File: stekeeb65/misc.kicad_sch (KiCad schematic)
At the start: 16 parts, among them J0 Conn_02x03_Odd_Even, J1 TYPE-C-31-M12_13_EDITED, U0 WE-TVS-82400102

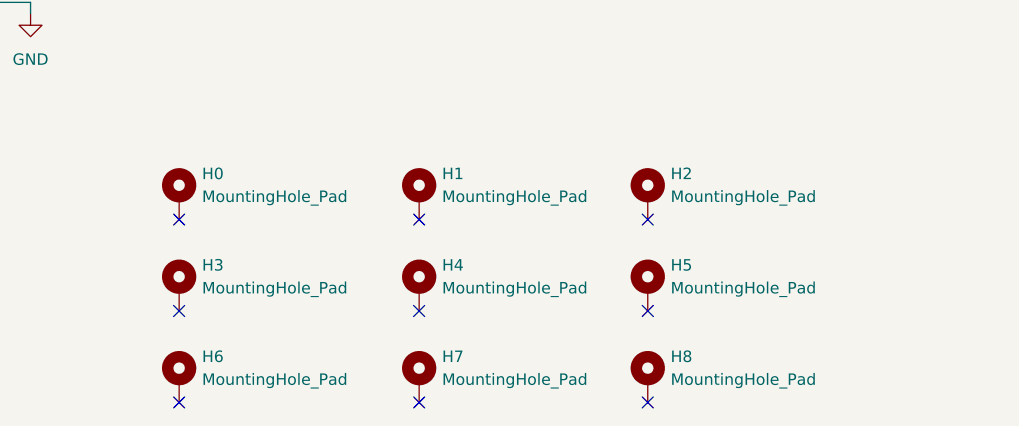
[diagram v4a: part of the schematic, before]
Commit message: Redoing keyboard layout. Adding flex cuts to PCB
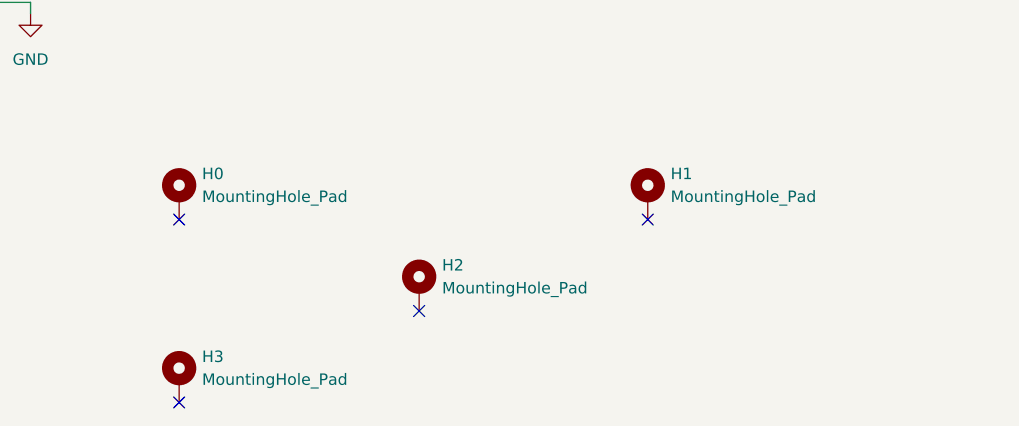
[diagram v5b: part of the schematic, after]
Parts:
- removed H1, H3, H5, H7, H8: MountingHole_Pad, MountingHole:MountingHole_2.2mm_M2_DIN965_Pad_TopOnly, symbol Mechanical:MountingHole_Pad
- F0: footprint Fuse:Fuse_0805_2012Metric_Pad1.15x1.40mm_HandSolder -> Fuse:Fuse_0603_1608Metric_Pad1.05x0.95mm_HandSolder
- H0: footprint MountingHole:MountingHole_2.2mm_M2_DIN965_Pad_TopOnly -> MountingHole:MountingHole_2.2mm_M2_DIN965_Pad_TopBottom
- H1: renamed from H2; footprint MountingHole:MountingHole_2.2mm_M2_DIN965_Pad_TopOnly -> MountingHole:MountingHole_2.2mm_M2_DIN965_Pad_TopBottom
- H2: renamed from H4; footprint MountingHole:MountingHole_2.2mm_M2_DIN965_Pad_TopOnly -> MountingHole:MountingHole_2.2mm_M2_DIN965_Pad_TopBottom
- H3: renamed from H6; footprint MountingHole:MountingHole_2.2mm_M2_DIN965_Pad_TopOnly -> MountingHole:MountingHole_2.2mm_M2_DIN965_Pad_TopBottom
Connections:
- no-connect marks 11 -> 6
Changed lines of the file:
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@@
   )
   (no_connect (at 91.44 135.89))
-  (no_connect (at 91.44 146.05))
-  (no_connect (at 116.84 135.89))
   (no_connect (at 116.84 125.73))
   (no_connect (at 64.77 125.73))
-  (no_connect (at 91.44 125.73))
   (no_connect (at 64.77 146.05))
-  (no_connect (at 116.84 146.05))
   (no_connect (at 54.61 92.71))
   (no_connect (at 54.61 90.17))
-  (no_connect (at 64.77 135.89))
   (wire (pts (xy 31.75 101.6) (xy 31.75 100.33))
     (stroke (width 0) (type default) (color 0 0 0 0))
@@
     (pin "1")
   )
-  (symbol (lib_id "Mechanical:MountingHole_Pad") (at 116.84 133.35 0) (unit 1)
-    (in_bom yes) (on_board yes) (fields_autoplaced)
-    (property "Reference" "H5" (id 0) (at 119.38 130.8099 0)
-      (effects (font (size 1.27 1.27)) (justify left))
-    )
-    (property "Value" "MountingHole_Pad" (id 1) (at 119.38 133.3499 0)
-      (effects (font (size 1.27 1.27)) (justify left))
-    )
-    (property "Footprint" "MountingHole:MountingHole_2.2mm_M2_DIN965_Pad_TopOnly" (id 2) (at 116.84 133.35 0)
-      (effects (font (size 1.27 1.27)) hide)
-    )
-    (property "Datasheet" "~" (id 3) (at 116.84 133.35 0)
-      (effects (font (size 1.27 1.27)) hide)
-    )
-    (pin "1")
-  )
   (symbol (lib_id "Mechanical:MountingHole_Pad") (at 64.77 123.19 0) (unit 1)
     (in_bom yes) (on_board yes) (fields_autoplaced)
@@
       (effects (font (size 1.27 1.27)) (justify left))
     )
-    (property "Footprint" "MountingHole:MountingHole_2.2mm_M2_DIN965_Pad_TopOnly" (id 2) (at 64.77 123.19 0)
+    (property "Footprint" "MountingHole:MountingHole_2.2mm_M2_DIN965_Pad_TopBottom" (id 2) (at 64.77 123.19 0)
       (effects (font (size 1.27 1.27)) hide)
     )
@@
     (pin "2")
   )
-  (symbol (lib_id "Mechanical:MountingHole_Pad") (at 91.44 123.19 0) (unit 1)
-    (in_bom yes) (on_board yes) (fields_autoplaced)
-    (property "Reference" "H1" (id 0) (at 93.98 120.6499 0)
-      (effects (font (size 1.27 1.27)) (justify left))
-    )
-    (property "Value" "MountingHole_Pad" (id 1) (at 93.98 123.1899 0)
-      (effects (font (size 1.27 1.27)) (justify left))
-    )
-    (property "Footprint" "MountingHole:MountingHole_2.2mm_M2_DIN965_Pad_TopOnly" (id 2) (at 91.44 123.19 0)
-      (effects (font (size 1.27 1.27)) hide)
-    )
-    (property "Datasheet" "~" (id 3) (at 91.44 123.19 0)
-      (effects (font (size 1.27 1.27)) hide)
-    )
-    (pin "1")
-  )
   (symbol (lib_id "power:+5V") (at 92.71 62.23 0) (unit 1)
     (in_bom yes) (on_board yes) (fields_autoplaced)
@@
   (symbol (lib_id "Mechanical:MountingHole_Pad") (at 91.44 133.35 0) (unit 1)
     (in_bom yes) (on_board yes) (fields_autoplaced)
-    (property "Reference" "H4" (id 0) (at 93.98 130.8099 0)
+    (property "Reference" "H2" (id 0) (at 93.98 130.8099 0)
       (effects (font (size 1.27 1.27)) (justify left))
     )
@@
       (effects (font (size 1.27 1.27)) (justify left))
     )
-    (property "Footprint" "MountingHole:MountingHole_2.2mm_M2_DIN965_Pad_TopOnly" (id 2) (at 91.44 133.35 0)
+    (property "Footprint" "MountingHole:MountingHole_2.2mm_M2_DIN965_Pad_TopBottom" (id 2) (at 91.44 133.35 0)
       (effects (font (size 1.27 1.27)) hide)
     )
@@
     (pin "1")
   )
-  (symbol (lib_id "Mechanical:MountingHole_Pad") (at 64.77 133.35 0) (unit 1)
-    (in_bom yes) (on_board yes) (fields_autoplaced)
-    (property "Reference" "H3" (id 0) (at 67.31 130.8099 0)
-      (effects (font (size 1.27 1.27)) (justify left))
-    )
-    (property "Value" "MountingHole_Pad" (id 1) (at 67.31 133.3499 0)
-      (effects (font (size 1.27 1.27)) (justify left))
-    )
-    (property "Footprint" "MountingHole:MountingHole_2.2mm_M2_DIN965_Pad_TopOnly" (id 2) (at 64.77 133.35 0)
-      (effects (font (size 1.27 1.27)) hide)
-    )
-    (property "Datasheet" "~" (id 3) (at 64.77 133.35 0)
-      (effects (font (size 1.27 1.27)) hide)
-    )
-    (pin "1")
-  )
-  (symbol (lib_id "Mechanical:MountingHole_Pad") (at 91.44 143.51 0) (unit 1)
-    (in_bom yes) (on_board yes) (fields_autoplaced)
-    (property "Reference" "H7" (id 0) (at 93.98 140.9699 0)
-      (effects (font (size 1.27 1.27)) (justify left))
-    )
-    (property "Value" "MountingHole_Pad" (id 1) (at 93.98 143.5099 0)
-      (effects (font (size 1.27 1.27)) (justify left))
-    )
-    (property "Footprint" "MountingHole:MountingHole_2.2mm_M2_DIN965_Pad_TopOnly" (id 2) (at 91.44 143.51 0)
-      (effects (font (size 1.27 1.27)) hide)
-    )
-    (property "Datasheet" "~" (id 3) (at 91.44 143.51 0)
-      (effects (font (size 1.27 1.27)) hide)
-    )
-    (pin "1")
-  )
-  (symbol (lib_id "Mechanical:MountingHole_Pad") (at 116.84 143.51 0) (unit 1)
-    (in_bom yes) (on_board yes) (fields_autoplaced)
-    (property "Reference" "H8" (id 0) (at 119.38 140.9699 0)
-      (effects (font (size 1.27 1.27)) (justify left))
-    )
-    (property "Value" "MountingHole_Pad" (id 1) (at 119.38 143.5099 0)
-      (effects (font (size 1.27 1.27)) (justify left))
-    )
-    (property "Footprint" "MountingHole:MountingHole_2.2mm_M2_DIN965_Pad_TopOnly" (id 2) (at 116.84 143.51 0)
-      (effects (font (size 1.27 1.27)) hide)
-    )
-    (property "Datasheet" "~" (id 3) (at 116.84 143.51 0)
-      (effects (font (size 1.27 1.27)) hide)
-    )
-    (pin "1")
-  )
   (symbol (lib_id "Mechanical:MountingHole_Pad") (at 64.77 143.51 0) (unit 1)
     (in_bom yes) (on_board yes) (fields_autoplaced)
-    (property "Reference" "H6" (id 0) (at 67.31 140.9699 0)
+    (property "Reference" "H3" (id 0) (at 67.31 140.9699 0)
       (effects (font (size 1.27 1.27)) (justify left))
     )
@@
       (effects (font (size 1.27 1.27)) (justify left))
     )
-    (property "Footprint" "MountingHole:MountingHole_2.2mm_M2_DIN965_Pad_TopOnly" (id 2) (at 64.77 143.51 0)
+    (property "Footprint" "MountingHole:MountingHole_2.2mm_M2_DIN965_Pad_TopBottom" (id 2) (at 64.77 143.51 0)
       (effects (font (size 1.27 1.27)) hide)
     )
@@
   (symbol (lib_id "Mechanical:MountingHole_Pad") (at 116.84 123.19 0) (unit 1)
     (in_bom yes) (on_board yes) (fields_autoplaced)
-    (property "Reference" "H2" (id 0) (at 119.38 120.6499 0)
+    (property "Reference" "H1" (id 0) (at 119.38 120.6499 0)
       (effects (font (size 1.27 1.27)) (justify left))
     )
@@
       (effects (font (size 1.27 1.27)) (justify left))
     )
-    (property "Footprint" "MountingHole:MountingHole_2.2mm_M2_DIN965_Pad_TopOnly" (id 2) (at 116.84 123.19 0)
+    (property "Footprint" "MountingHole:MountingHole_2.2mm_M2_DIN965_Pad_TopBottom" (id 2) (at 116.84 123.19 0)
       (effects (font (size 1.27 1.27)) hide)
     )
@@
     (property "Reference" "F0" (id 0) (at 66.04 27.94 90))
     (property "Value" "Polyfuse" (id 1) (at 66.04 30.48 90))
-    (property "Footprint" "Fuse:Fuse_0805_2012Metric_Pad1.15x1.40mm_HandSolder" (id 2) (at 71.12 33.02 0)
+    (property "Footprint" "Fuse:Fuse_0603_1608Metric_Pad1.05x0.95mm_HandSolder" (id 2) (at 71.12 33.02 0)
       (effects (font (size 1.27 1.27)) (justify left) hide)
     )

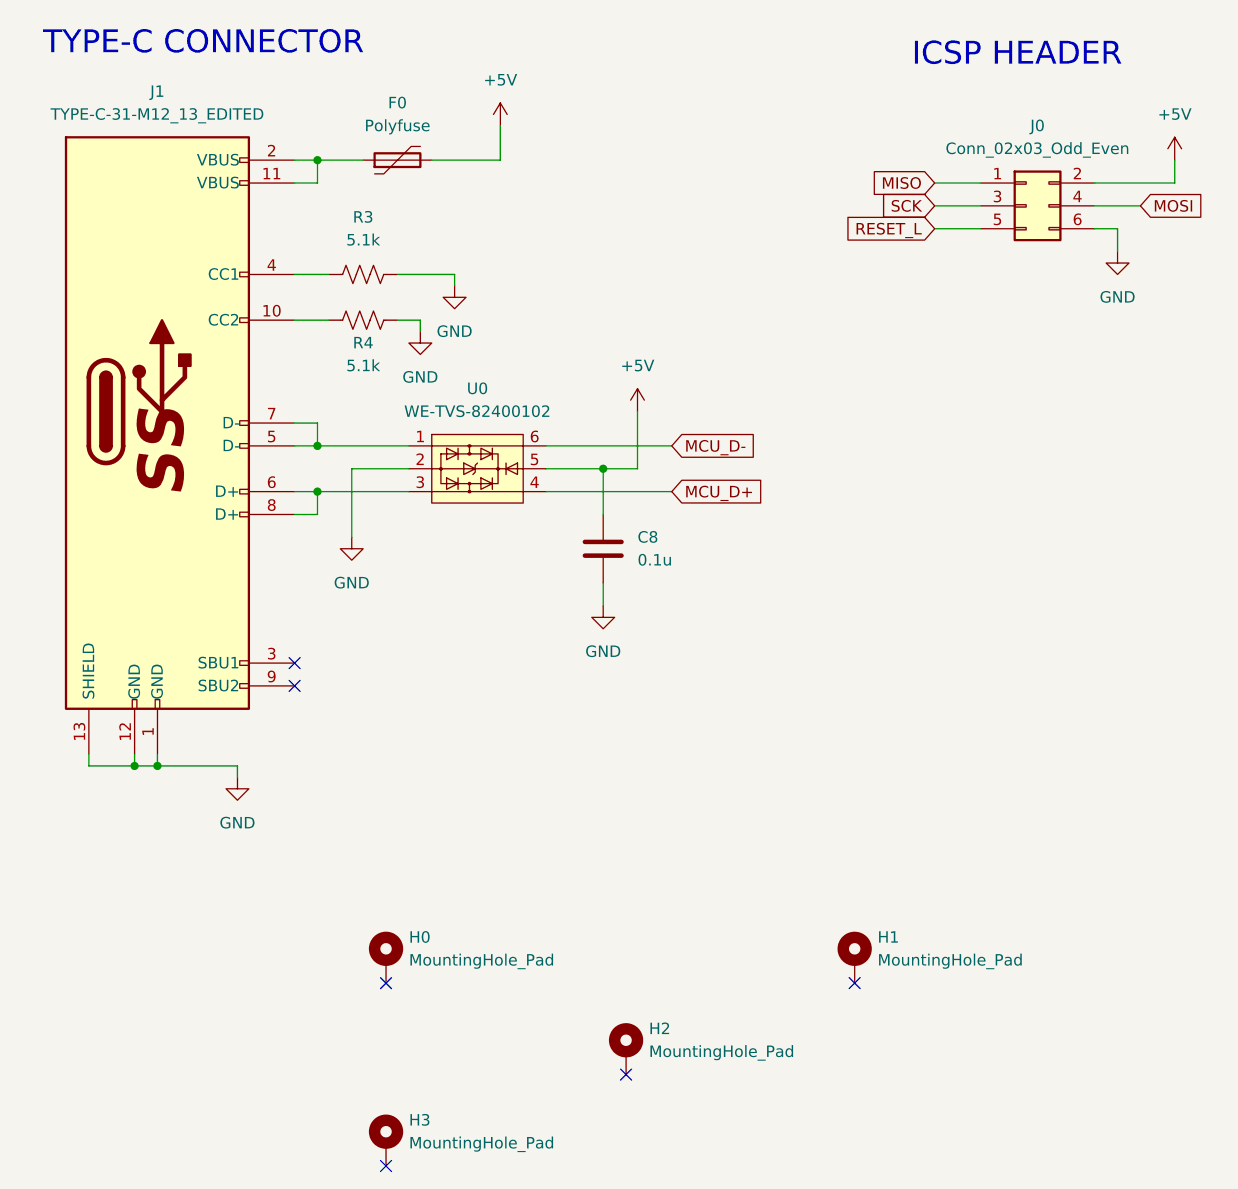
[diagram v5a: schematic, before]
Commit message: Replacing Type-C in lieu of a daughter board connector.
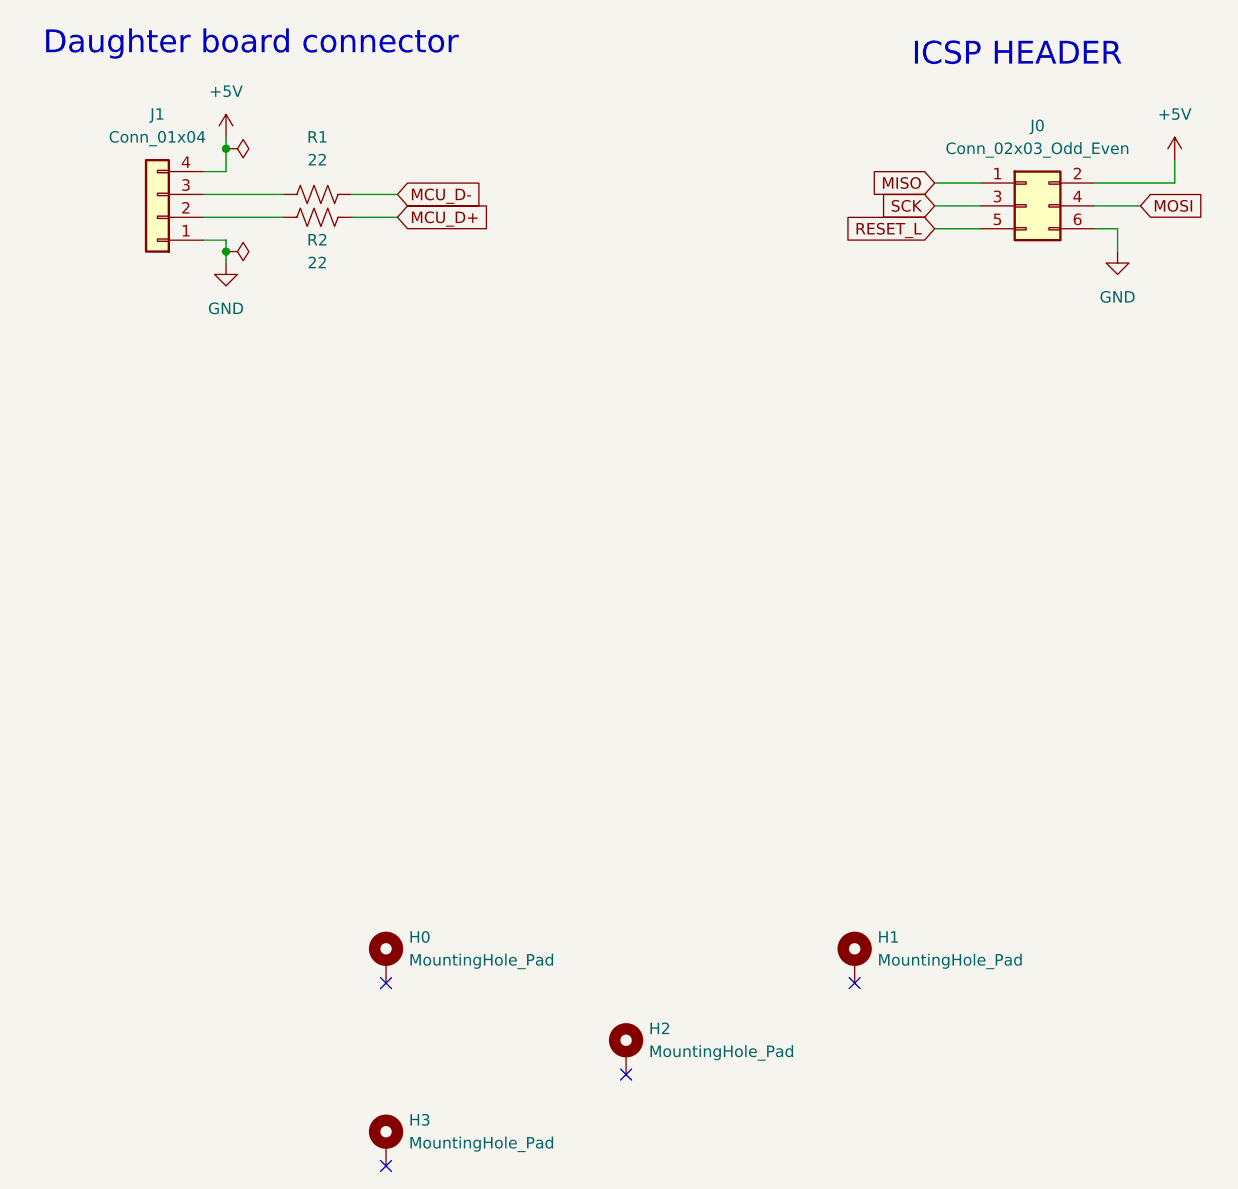
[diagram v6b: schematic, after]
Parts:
- removed C8: 0.1u, Capacitor_SMD:C_0603_1608Metric_Pad1.08x0.95mm_HandSolder, symbol Device:C
- removed F0: Polyfuse, Fuse:Fuse_0603_1608Metric_Pad1.05x0.95mm_HandSolder, symbol Device:Polyfuse
- removed J1: TYPE-C-31-M12_13_EDITED, Type-C:HRO-TYPE-C-31-M-12-Assembly, symbol mini_random_library:TYPE-C-31-M12_13_EDITED
- removed R3, R4: 5.1k, Resistor_SMD:R_0603_1608Metric_Pad0.98x0.95mm_HandSolder, symbol Device:R_US
- removed U0: WE-TVS-82400102, Package_TO_SOT_SMD:SOT-23-6, symbol Power_Protection:WE-TVS-82400102
- added J1: Conn_01x04, Connector_JST:JST_SH_SM04B-SRSS-TB_1x04-1MP_P1.00mm_Horizontal, symbol Connector_Generic:Conn_01x04
- added R1, R2: 22, Resistor_SMD:R_0603_1608Metric_Pad0.98x0.95mm_HandSolder, symbol Device:R_US
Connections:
- net +5V: now also J1.4 (Pin_4)
- net GND: now also J1.1 (Pin_1)
- net MCU_D+: now also R2.1
- net MCU_D-: now also R1.2
- new net: J1.3 (Pin_3), R1.1
- new net: J1.2 (Pin_2), R2.2
- no-connect marks 6 -> 4
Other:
- note added: "Daughter board connector"
- note removed: "TYPE-C CONNECTOR"
